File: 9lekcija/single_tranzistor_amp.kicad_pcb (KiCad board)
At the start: 2 copper layers, 31.2 x 25.7 mm, 11 parts, among them P1 PWR_CONN, P2 SIGNAL_IN, P3 SIGNAL_OUT, Q1 BC548

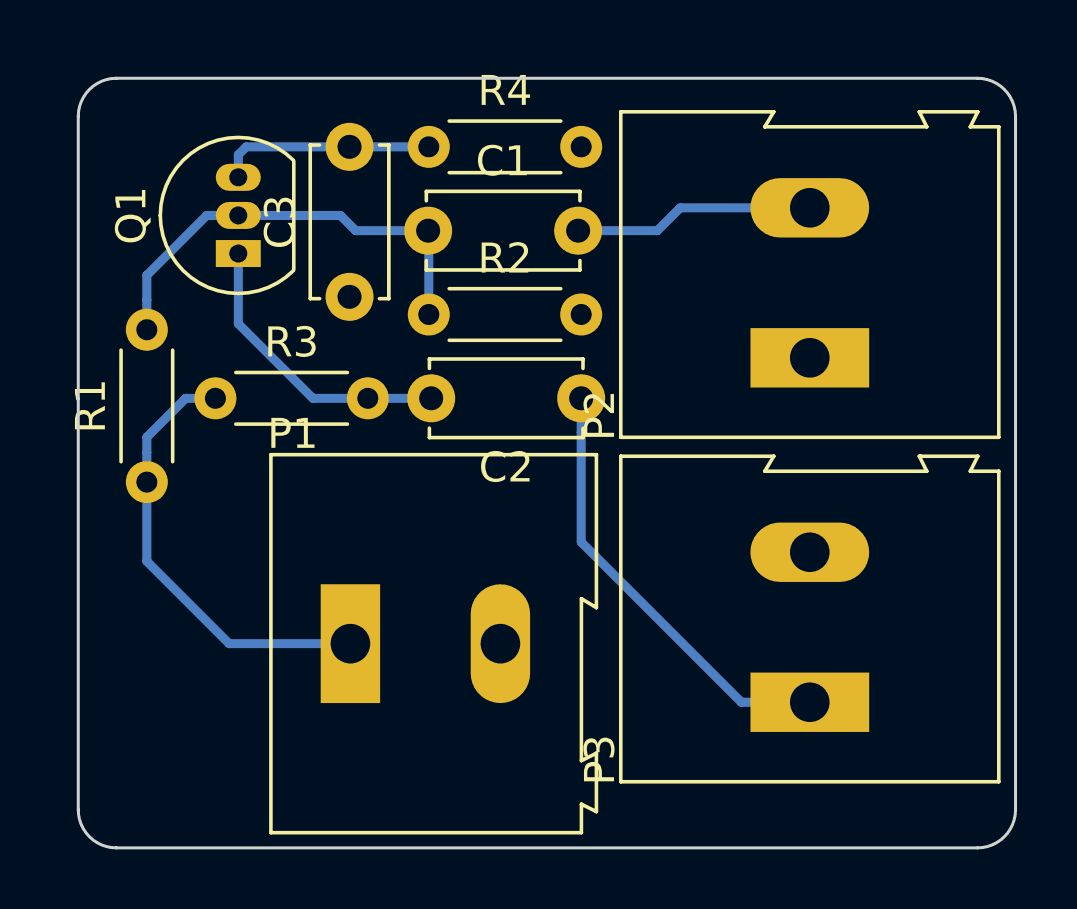
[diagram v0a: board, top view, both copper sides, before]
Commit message: Kursa darba papildinajums, lekciju darbu nobeigums
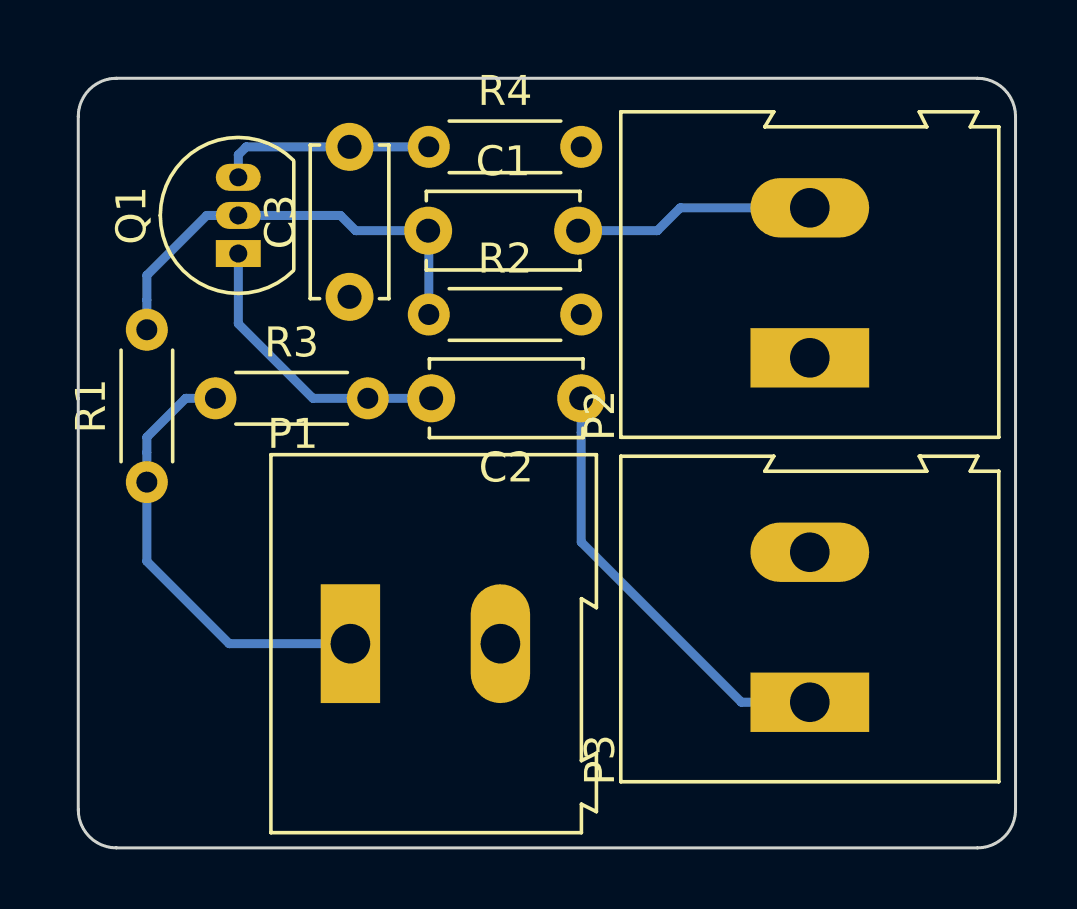
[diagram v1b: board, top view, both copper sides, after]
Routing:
- added copper zone on F.Cu, net GND
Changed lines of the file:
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@@
   (general
     (links 16)
-    (no_connects 10)
-    (area 164.287999 83.007999 195.630001 108.762001)
+    (no_connects 0)
+    (area 163.489 82.209 197.847 111.0298)
     (thickness 1.6)
     (drawings 12)
@@
     (33 F.Adhes user hide)
     (35 F.Paste user hide)
-    (37 F.SilkS user hide)
+    (37 F.SilkS user)
     (39 F.Mask user hide)
     (40 Dwgs.User user hide)
@@
     (pad_to_mask_clearance 0)
     (aux_axis_origin 0 0)
-    (visible_elements 7FFFEFDF)
+    (visible_elements 7FFFE7DF)
     (pcbplotparams
       (layerselection 0x00030_80000001)
@@
     (connect_pads (clearance 0.508))
     (min_thickness 0.254)
+    (fill yes (mode segment) (arc_segments 32) (thermal_gap 0.508) (thermal_bridge_width 0.508))
+    (polygon
+      (pts
+        (xy 194.31 108.712) (xy 194.564 108.712) (xy 195.072 108.458) (xy 195.326 108.204) (xy 195.58 107.696)
+        (xy 195.58 107.442) (xy 195.58 84.074) (xy 195.326 83.566) (xy 195.072 83.312) (xy 194.564 83.058)
+        (xy 165.354 83.058) (xy 164.846 83.312) (xy 164.592 83.566) (xy 164.338 84.074) (xy 164.338 107.696)
+        (xy 164.592 108.204) (xy 164.846 108.458) (xy 165.354 108.712)
+      )
+    )
+  )
+  (zone (net 5) (net_name GND) (layer F.Cu) (hatch edge 0.508)
+    (connect_pads (clearance 0.508))
+    (min_thickness 0.254)
